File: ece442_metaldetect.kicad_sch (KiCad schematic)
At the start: 33 parts

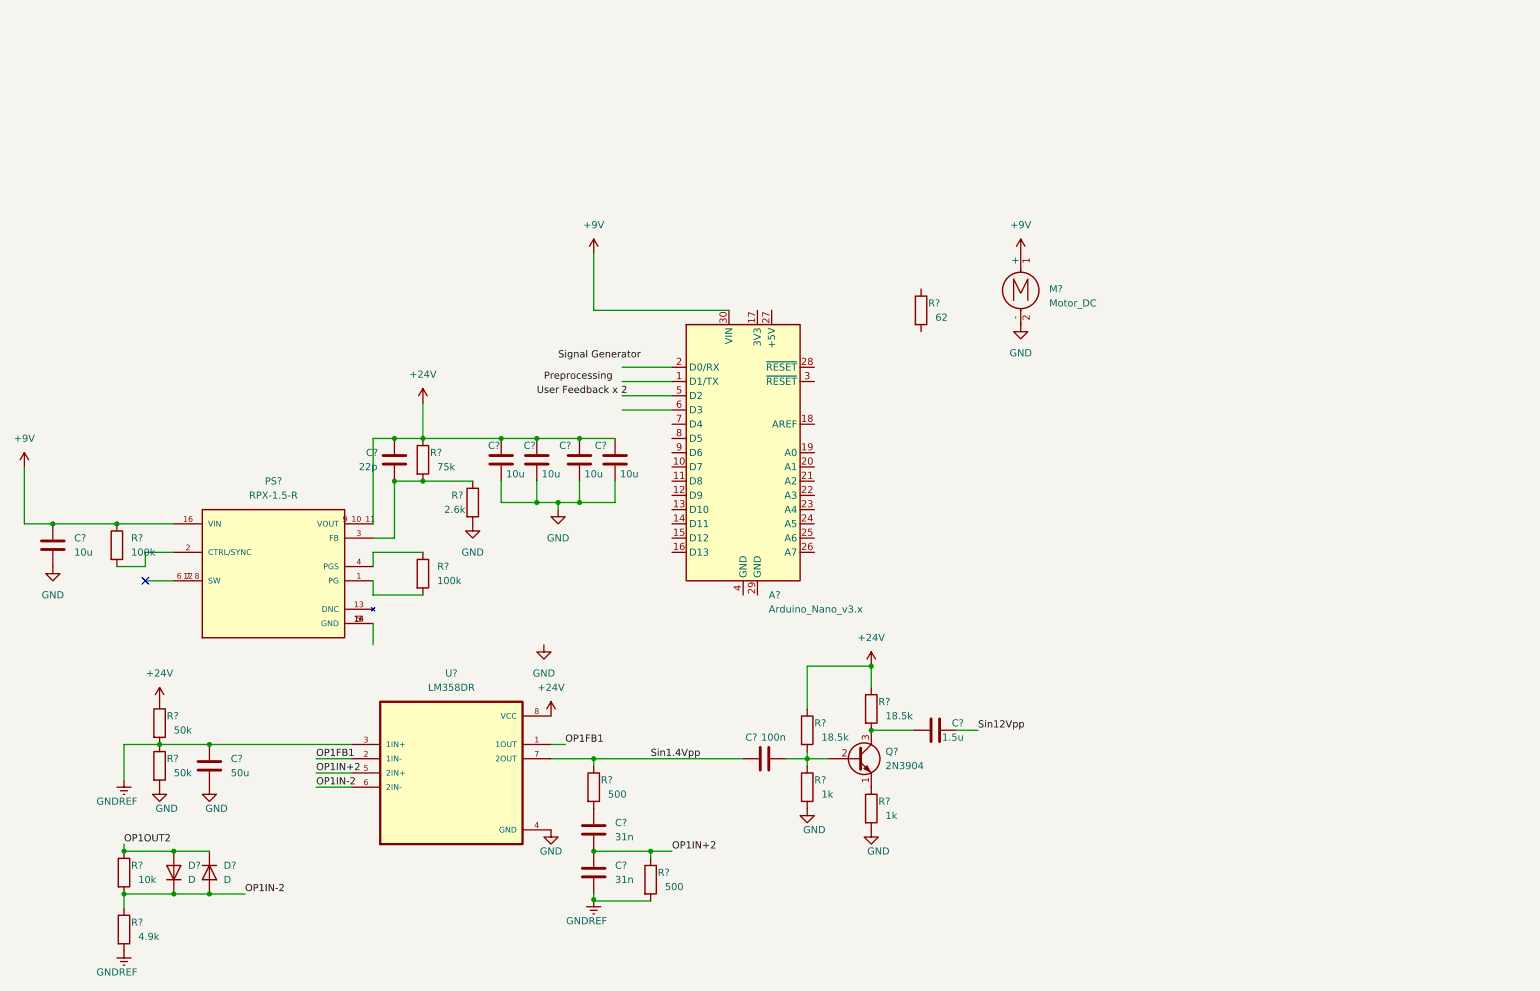
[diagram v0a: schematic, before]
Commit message: Add files via upload
Added Coil and User Feedback modules, added BOM for respective parts
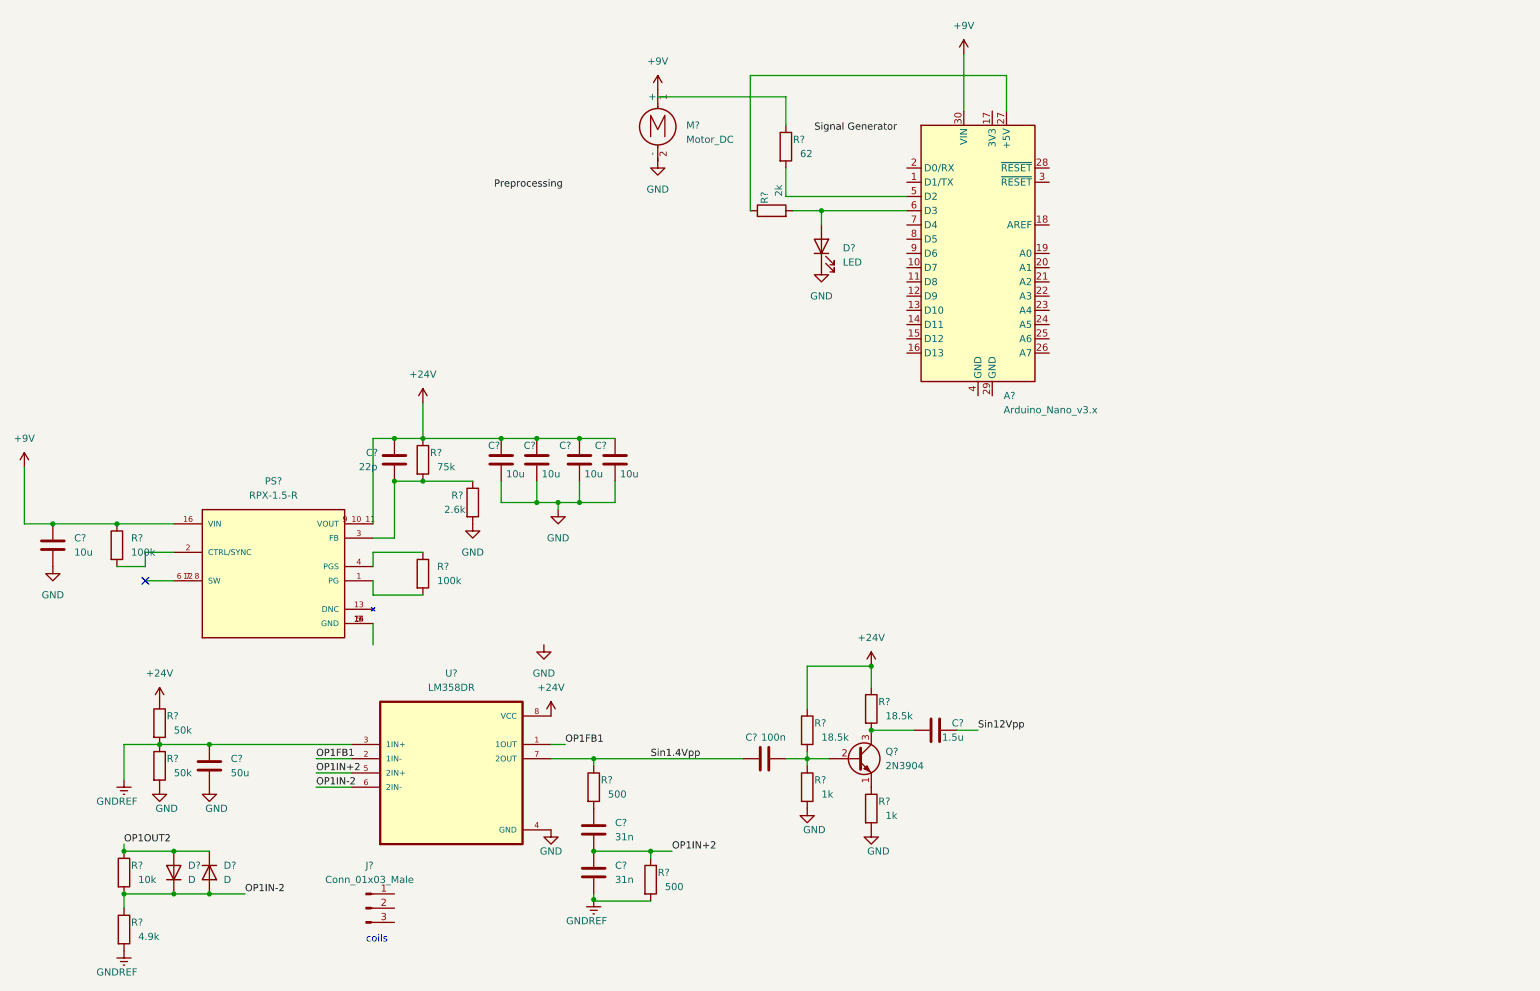
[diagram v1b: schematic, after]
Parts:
- added D?: LED, LED_THT:LED_Rectangular_W5.0mm_H2.0mm, symbol Device:LED
- added J?: Conn_01x03_Male, Connector_PinHeader_2.54mm:PinHeader_1x03_P2.54mm_Horizontal, symbol Connector:Conn_01x03_Male
- added R?: 2k, Resistor_SMD:R_0805_2012Metric, symbol Device:R
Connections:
- net GND: now also D?.1 (K)
- net at R?.2: now also A?.5 (D2)
- net at A?.27 (+5V): now also R?.1
- net at A?.6 (D3): now also D?.2 (A), R?.2
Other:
- note added: "coils"
- moved on the sheet: A?, M?, R?

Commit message: Add files via upload
added test points to design, critique accordingly
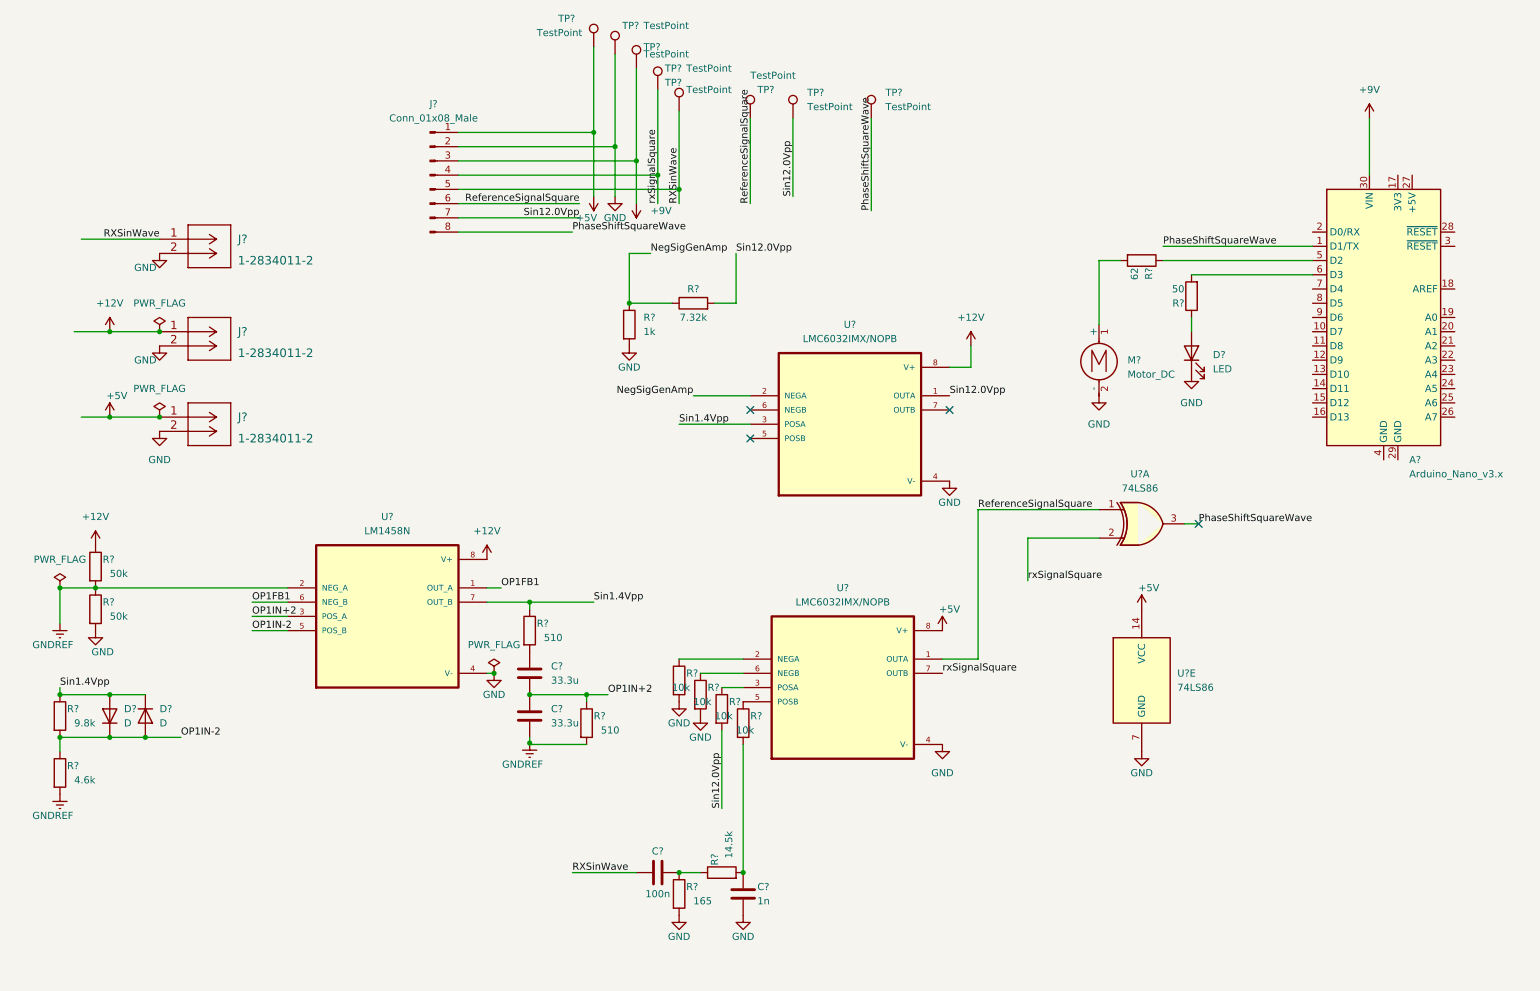
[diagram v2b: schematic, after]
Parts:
- removed C?: 22p, Capacitor_SMD:C_0805_2012Metric, symbol Device:C
- removed C? (x5): 10u, Capacitor_SMD:C_0805_2012Metric, symbol Device:C
- removed C?: 1.5u, Capacitor_SMD:C_0805_2012Metric, symbol Device:C
- removed C? (x2): 31n, Capacitor_SMD:C_0805_2012Metric, symbol Device:C
- removed C?: 100n, Capacitor_SMD:C_0805_2012Metric, symbol Device:C
- removed C?: 50u, Capacitor_SMD:C_0805_2012Metric, symbol Device:C
- removed D? (x2): D, Diode_SMD:D_0805_2012Metric, symbol Device:D
- removed J?: Conn_01x03_Male, Connector_PinHeader_2.54mm:PinHeader_1x03_P2.54mm_Horizontal, symbol Connector:Conn_01x03_Male
- removed PS?: RPX-1.5-R, RPX-1:CONV_RPX-1.5-R, symbol RPX-1.5-R:RPX-1.5-R
- removed Q?: 2N3904, Package_TO_SOT_THT:TO-92_Inline, symbol Transistor_BJT:2N3904
- removed R?: 62, Resistor_SMD:R_0805_2012Metric, symbol Device:R
- removed R? (x2): 18.5k, Resistor_SMD:R_0805_2012Metric, symbol Device:R
- removed R? (x2): 1k, Resistor_SMD:R_0805_2012Metric, symbol Device:R
- removed R? (x2): 100k, Resistor_SMD:R_0805_2012Metric, symbol Device:R
- removed R?: 2.6k, Resistor_SMD:R_0805_2012Metric, symbol Device:R
- removed R?: 75k, Resistor_SMD:R_0805_2012Metric, symbol Device:R
- removed R?: 4.9k, Resistor_SMD:R_0805_2012Metric, symbol Device:R
- removed R?: 2k, Resistor_SMD:R_0805_2012Metric, symbol Device:R
- removed R?: 10k, Resistor_SMD:R_0805_2012Metric, symbol Device:R
- removed R? (x2): 50k, Resistor_SMD:R_0805_2012Metric, symbol Device:R
- removed R? (x2): 500, Resistor_SMD:R_0805_2012Metric, symbol Device:R
- removed U?: LM358DR, LM358DR:SOIC127P599X175-8N, symbol LM358DR:LM358DR
- added C?: 1n, Capacitor_SMD:C_0402_1005Metric, symbol Device:C
- added C?: 100n, Capacitor_SMD:C_0402_1005Metric, symbol Device:C
- added C? (x2): 33.3u, Capacitor_THT:C_Rect_L7.0mm_W3.5mm_P5.00mm, symbol Device:C
- added D? (x2): D, Diode_THT:D_DO-35_SOD27_P7.62mm_Horizontal, symbol Device:D
- added J? (x3): 1-2834011-2, 1-2834011-2:1-2834011-2, symbol 1-2834011-2:1-2834011-2
- added J?: Conn_01x08_Male, Connector_PinHeader_2.54mm:PinHeader_1x08_P2.54mm_Horizontal, symbol Connector:Conn_01x08_Male
- added R?: 1k, Resistor_SMD:R_1206_3216Metric, symbol Device:R
- added R?: 14.5k, Resistor_SMD:R_0805_2012Metric, symbol Device:R
- added R? (x4): 10k, Resistor_SMD:R_0805_2012Metric, symbol Device:R
- added R?: 165, Resistor_SMD:R_1206_3216Metric, symbol Device:R
- added R?: 9.8k, Resistor_SMD:R_0805_2012Metric, symbol Device:R
- added R?: 50, Resistor_SMD:R_0805_2012Metric, symbol Device:R
- added R? (x2): 50k, Resistor_SMD:R_1206_3216Metric, symbol Device:R
- added R?: 4.6k, Resistor_SMD:R_0603_1608Metric, symbol Device:R
- added R? (x2): 510, Resistor_SMD:R_0603_1608Metric, symbol Device:R
- added R?: 7.32k, Resistor_SMD:R_0805_2012Metric, symbol Device:R
- added R?: 62, Resistor_SMD:R_0805_2012Metric, symbol Device:R
- added TP? (x8): TestPoint, symbol Connector:TestPoint
- added U? (x2): LMC6032IMX/NOPB, LMC6032IMX_NOPB:SOIC127P599X175-8N, symbol LMC6032:LMC6032IMX/NOPB
- added U? (x2): 74LS86, Package_SO:SOIC-14_3.9x8.7mm_P1.27mm, symbol 74xx:74LS86
- added U?: LM1458N, LM1458N:DIP794W45P254L959H508Q8, symbol LM1458N:LM1458N
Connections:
- net +9V: now also J?.3 (Pin_3), TP?.1; no longer M?.1 (+)
- net GND: now also C?.1, J?.2, J?.2, J?.2, J?.2 (Pin_2), R?.2, R?.2, R?.2, R?.2, R?.2, TP?.1, U?.4 (V-), U?.4 (V-), U?.4 (V-), U?.7 (GND)
- net GNDREF: now also C?.2, R?.1, R?.2, R?.2, R?.2, U?.2 (NEG_A)
- net OP1FB1: now also U?.1 (OUT_A), U?.6 (NEG_B)
- net OP1IN+2: now also C?.1, C?.2, R?.1, U?.3 (POS_A)
- net OP1IN-2: now also D?.1 (K), D?.2 (A), R?.1, R?.2, U?.5 (POS_B)
- net Sin1.4Vpp: now also D?.1 (K), D?.2 (A), R?.1, R?.1, U?.3 (POSA), U?.7 (OUT_B)
- net at A?.5 (D2): now also R?.1
- net at D?.2 (A): now also R?.1; no longer A?.6 (D3)
- net PhaseShiftSquareWave: now reaches A?.1 (D1/TX)
- net PhaseShiftSquareWave: now also J?.8 (Pin_8), TP?.1, U?.3
- new net: R?.1, U?.2 (NEGA)
- new net: R?.1, U?.3 (POSA)
- new net: R?.1, U?.5 (POSB)
- new net: R?.1, U?.6 (NEGB)
- new net: C?.2, R?.1, R?.1
- new net: C?.2, R?.2, R?.2
- new net: M?.1 (+), R?.2
- new net: A?.6 (D3), R?.2
- new net: C?.1, R?.2
- new net +12V: J?.1, R?.1, U?.8 (V+), U?.8 (V+)
- new net +5V: J?.1, J?.1 (Pin_1), TP?.1, U?.14 (VCC), U?.8 (V+)
- new net NegSigGenAmp: R?.1, R?.1, U?.2 (NEGA)
- new net RXSinWave: C?.1, J?.1, J?.5 (Pin_5), TP?.1
- new net ReferenceSignalSquare: J?.6 (Pin_6), TP?.1, U?.1, U?.1 (OUTA)
- new net Sin12.0Vpp: J?.7 (Pin_7), R?.2, R?.2, TP?.1, U?.1 (OUTA)
- new net rxSignalSquare: J?.4 (Pin_4), TP?.1, U?.2, U?.7 (OUTB)
- no-connect marks 1 -> 4
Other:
- note removed: "coils"
- moved on the sheet: A?, D?, M?

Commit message: Add files via upload
first version pcb done, may need changes
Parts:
- removed TP? (x8): TestPoint, symbol Connector:TestPoint
- added C10, C11, C12, C5, C6, C7, C8, C9: 100n, Capacitor_SMD:C_0402_1005Metric, symbol Device:C
- gave numbers to parts that had none: 33

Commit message: Add files via upload
the actual changes made
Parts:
- removed C11: 100n, Capacitor_SMD:C_0402_1005Metric, symbol Device:C
- removed J1, J2, J3: 1-2834011-2, 1-2834011-2:1-2834011-2, symbol 1-2834011-2:1-2834011-2
- removed U2, U3: LMC6032IMX/NOPB, LMC6032IMX_NOPB:SOIC127P599X175-8N, symbol LMC6032:LMC6032IMX/NOPB
- added J1, J2: 1-2834011-2, TestPoint:connect_detect, symbol 2023-03-08_22-40-49:1-2834011-2
- added J3: Conn_01x03_Male, Connector_PinHeader_2.54mm:PinHeader_1x03_P2.54mm_Horizontal, symbol Connector:Conn_01x03_Male
- added J5, J6: Screw_Terminal_01x02, Connector_PinHeader_2.54mm:PinHeader_1x02_P2.54mm_Vertical, symbol Connector:Screw_Terminal_01x02
- added U2, U3: LMC6032IMX/NOPB, SOIC127P599X175-8N, symbol LMC6032IMX_NOPB:LMC6032IMX/NOPB
- C10, C12, C3, C4, C5, C6, C7, C8, C9: footprint Capacitor_SMD:C_0402_1005Metric -> Capacitor_SMD:C_0805_2012Metric
- M1: footprint libraries:VCLP0820B004L_Vibrator -> TestPoint:vclp_vibrator
- U1: footprint LM1458N:DIP794W45P254L959H508Q8 -> TestPoint:DIP794-detect; PurchaseLink https://www.digikey.com/en/products/detail/texas-instrument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 -> (none)
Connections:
- net +12V: now also C10.1, C6.1, C7.1, J2.1, U3.8 (V+)
- net +5V: now also A1.27 (+5V), C12.1, C8.2, C9.1, U2.8 (V+)
- net +9V: now also C5.1, J5.1 (Pin_1)
- net GND: now also A1.29 (GND), A1.4 (GND), C10.2, C12.2, C5.2, C6.2, C7.2, C8.1, C9.2, J1.2, J2.2, J3.2 (Pin_2), J5.2 (Pin_2), J6.2 (Pin_2), U2.4 (V-), U3.4 (V-)
- net NegSigGenAmp: now also U3.2 (NEGA)
- net RXSinWave: now also J1.1, J3.3 (Pin_3)
- net ReferenceSignalSquare: now also U2.1 (OUTA)
- net Sin1.4Vpp: now also U3.3 (POSA)
- net Sin12.0Vpp: now also J3.1 (Pin_1), U3.1 (OUTA)
- net rxSignalSquare: now also U2.7 (OUTB)
- net at R8.1: now also U2.2 (NEGA)
- net at R12.1: now also U2.3 (POSA)
- net at R14.1: now also U2.5 (POSB)
- net at R11.1: now also U2.6 (NEGB)
- net at M1.1 (+), R15.2: now also J6.1 (Pin_1)
- no-connect marks 4 -> 26
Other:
- note added: "Coil Connection"
